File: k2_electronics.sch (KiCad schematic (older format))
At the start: 62 parts, among them J1 Conn_02x03_Odd_Even, Q1 Q_NMOS_GSD, SW1 SW_SPST, SW10 SW_SPST, SW11 SW_SPST, SW12 SW_SPST, SW13 SW_SPST, SW14 SW_SPST, SW15 SW_SPST, SW16 SW_SPST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

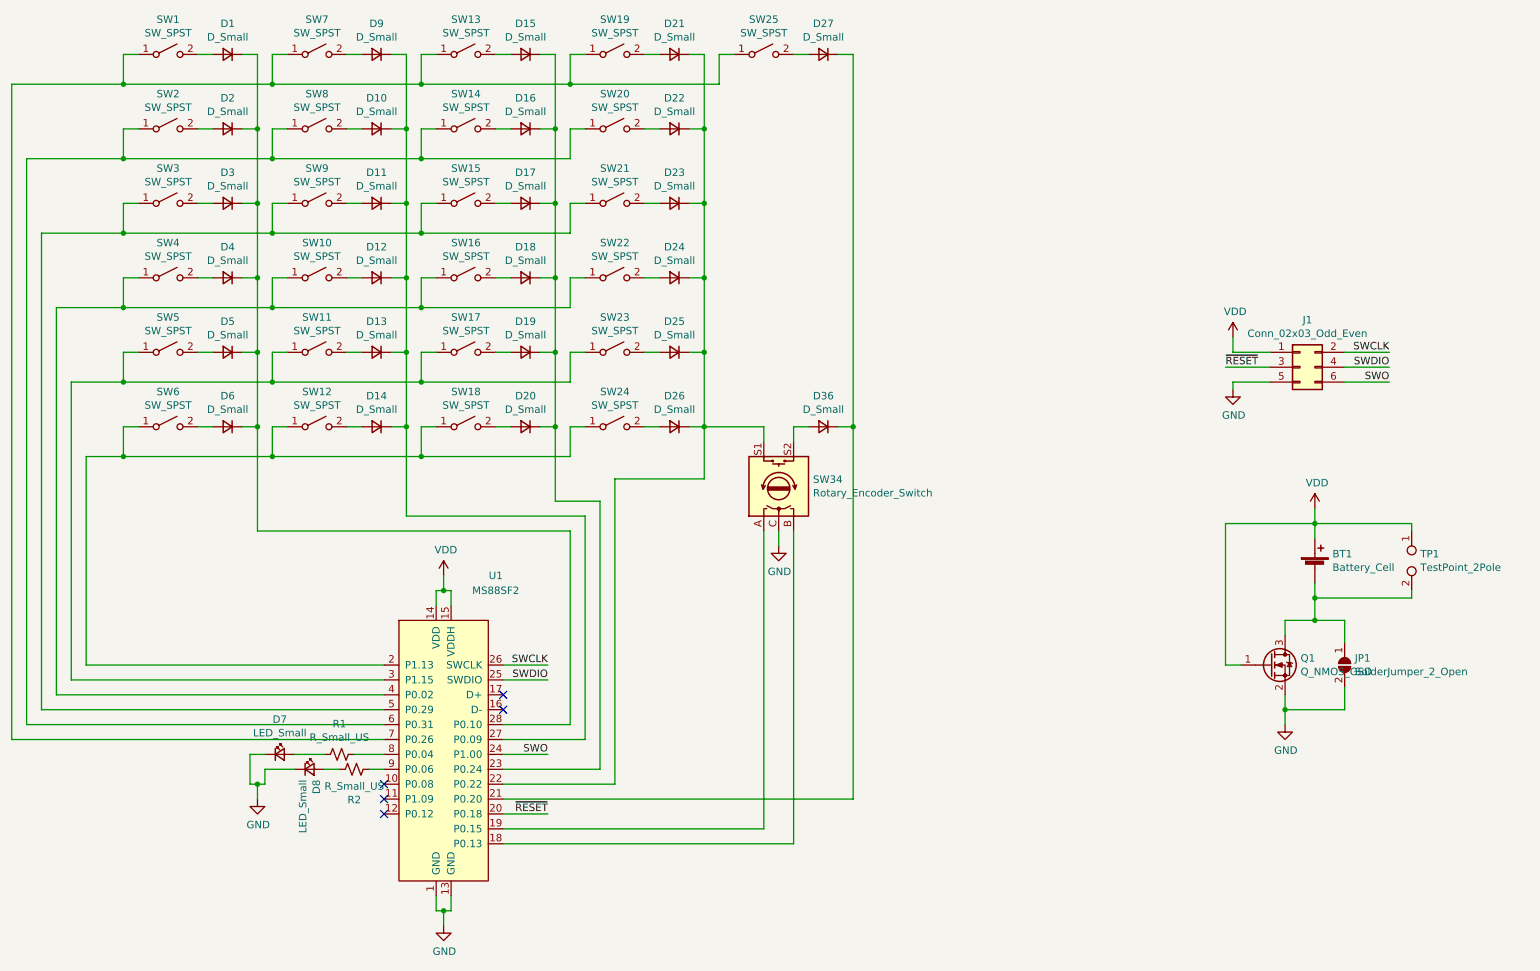
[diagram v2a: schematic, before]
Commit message: PCB mount
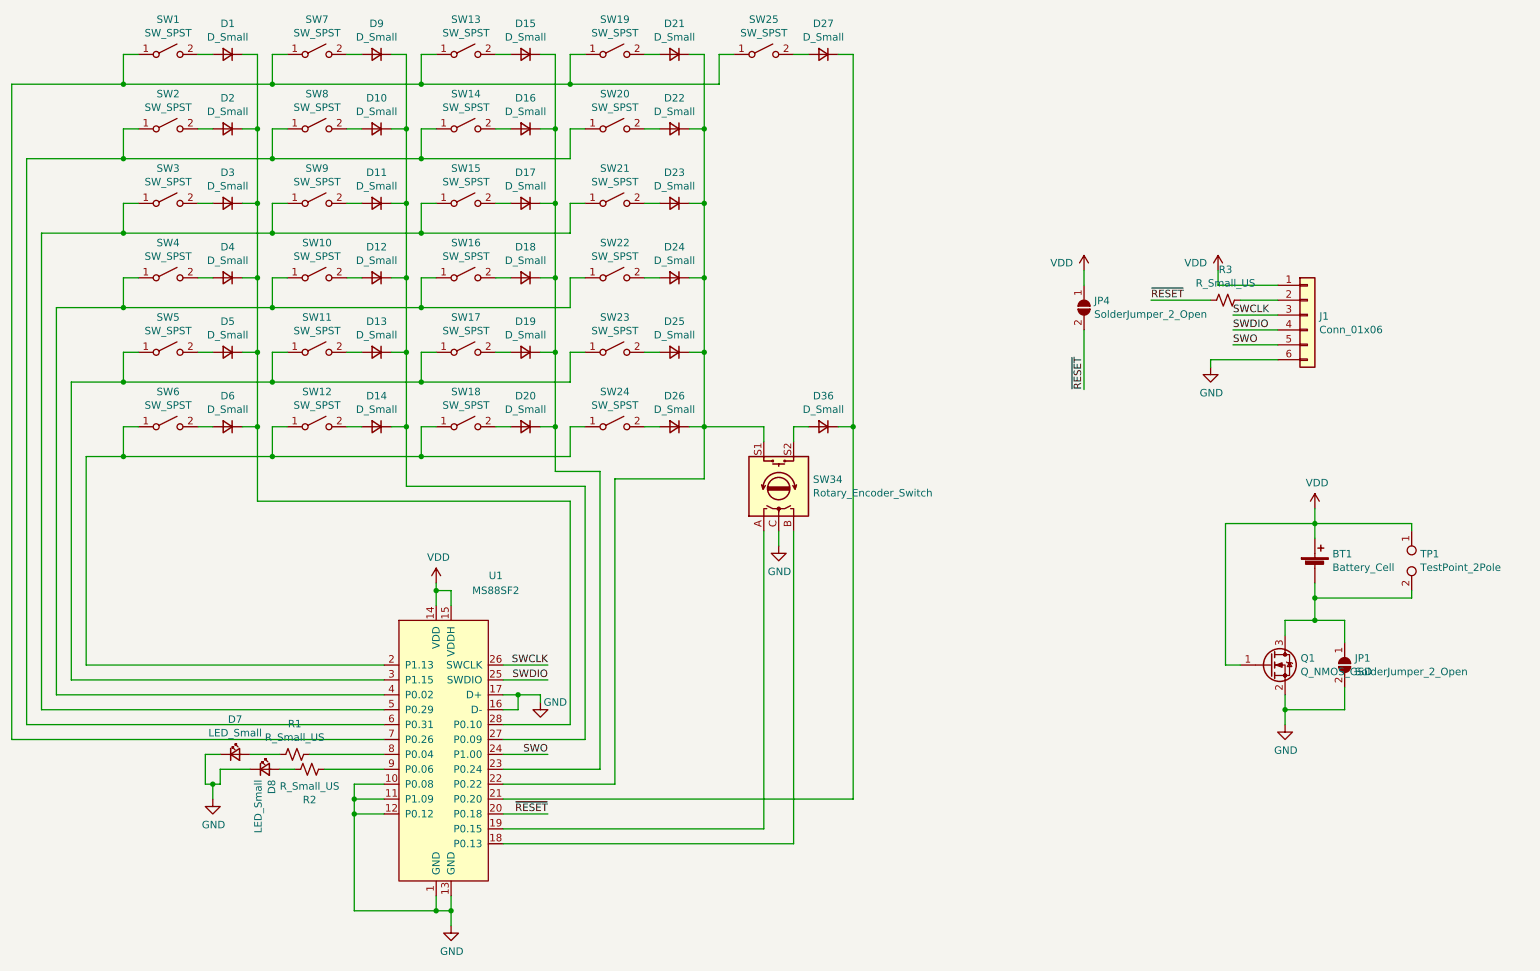
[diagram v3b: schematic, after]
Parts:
- removed J1: Conn_02x03_Odd_Even, Connector_PinHeader_2.54mm:PinHeader_2x03_P2.54mm_Vertical, symbol Connector_Generic:Conn_02x03_Odd_Even
- added J1: Conn_01x06, k2:PinHeader_1x06_P2.54mm_Horizontal, symbol Connector_Generic:Conn_01x06
- added JP4: SolderJumper_2_Open, k2:SolderJumper-2_P1.3mm_Open_Pad1.0x1.5mm_reversible, symbol Jumper:SolderJumper_2_Open
- added R3: R_Small_US, k2:R_0603_1608Metric_Pad0.98x0.95mm_HandSolder_reversible, symbol Device:R_Small_US
- SW34: footprint Rotary_Encoder:RotaryEncoder_Alps_EC11E-Switch_Vertical_H20mm -> k2:RotaryEncoder_Alps_EC11E-Switch_Vertical_H20mm
- TP1: footprint TestPoint:TestPoint_2Pads_Pitch2.54mm_Drill0.8mm -> k2:TestPoint_2Pads_Pitch2.54mm_Drill0.8mm
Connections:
- net GND: now also U1.10 (P0.08), U1.11 (P1.09), U1.12 (P0.12), U1.16 (D-), U1.17 (D+), J1.6 (Pin_6)
- net SWCLK: now also J1.3 (Pin_3)
- net SWDIO: now also J1.4 (Pin_4)
- net SWO: now also J1.5 (Pin_5)
- net VDD: now also J1.1 (Pin_1), JP4.1 (A)
- net ~RESET: now also JP4.2 (B), R3.1
- new net: J1.2 (Pin_2), R3.2
- no-connect marks 5 -> 0
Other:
- moved on the sheet: D7, D8, R1, R2
